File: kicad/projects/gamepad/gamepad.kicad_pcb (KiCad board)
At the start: 2 copper layers, 203.2 x 97.8 mm, 49 parts, among them J1 peripheral_addr_bus_connector, J2 peripheral_aux_connector, J3 peripheral_membank_connector, J4 Conn_01x02_Socket, J5 Conn_01x02_Socket, J6 Conn_02x05_Odd_Even, U1 74HC161, U10 74HC245, U11 74HC245, U12 74HC245, U13 74HC245, U2 74HC161, U3 74HC595, U4 74HC595, U5 74HC595, U6 74HC595, U7 74HC14, U8 74HC08, U9 74HC109

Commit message: Gamepad schematic done.
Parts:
- added C10: C, Capacitor_THT:C_Disc_D5.0mm_W2.5mm_P5.00mm, F.Cu at (116.8, 86.4)
- added C11: C, Capacitor_THT:C_Disc_D5.0mm_W2.5mm_P5.00mm, F.Cu at (129.6, 86.4)
- added C12: C, Capacitor_THT:C_Disc_D5.0mm_W2.5mm_P5.00mm, F.Cu at (182.9, 109.2)
- added C13: C, Capacitor_THT:C_Disc_D5.0mm_W2.5mm_P5.00mm, F.Cu at (215.9, 109.2)
- added C14: C, Capacitor_THT:C_Disc_D5.0mm_W2.5mm_P5.00mm, F.Cu at (147.3, 124.5)
- added J10: Pad 2 SNES, Connector_PinSocket_2.54mm:PinSocket_1x05_P2.54mm_Horizontal, F.Cu at (129.5, 61.0)
- added J11: Conn_01x03_Pin, Connector_PinHeader_2.54mm:PinHeader_1x03_P2.54mm_Horizontal, F.Cu at (52.5, 127.5)
- added J7: Pad 1 header, Connector_PinSocket_2.54mm:PinSocket_1x05_P2.54mm_Horizontal, F.Cu at (61.0, 88.9)
- added J8: Pad 1 SNES, Connector_PinSocket_2.54mm:PinSocket_1x05_P2.54mm_Horizontal, F.Cu at (81.3, 61.0)
- added J9: Pad 2 header, Connector_PinSocket_2.54mm:PinSocket_1x05_P2.54mm_Horizontal, F.Cu at (61.0, 109.2)
- added R3: 10K, Resistor_THT:R_Axial_DIN0207_L6.3mm_D2.5mm_P10.16mm_Horizontal, F.Cu at (160.0, 78.7)
- added TP1: Gamepad Latch, Connector_Pin:Pin_D1.0mm_L10.0mm, F.Cu at (-38.1, 28.5)
- added TP2: Shift out reg CLK, Connector_Pin:Pin_D1.0mm_L10.0mm, F.Cu at (-38.1, 32.5)
- added TP3: Shift Serial CLK, Connector_Pin:Pin_D1.0mm_L10.0mm, F.Cu at (-38.1, 36.6)
- added TP4: Gamepad CLK, Connector_Pin:Pin_D1.0mm_L10.0mm, F.Cu at (-38.1, 40.6)
- added TP5: Base CLK, Connector_Pin:Pin_D1.0mm_L10.0mm, F.Cu at (-34.0, 28.5)
- added TP6: ~{Base CLK}, Connector_Pin:Pin_D1.0mm_L10.0mm, F.Cu at (-34.0, 32.5)
- added TP7: RCO, Connector_Pin:Pin_D1.0mm_L10.0mm, F.Cu at (-34.0, 36.6)
- added U14: 74HC00, Package_DIP:DIP-14_W7.62mm_Socket, F.Cu at (152.4, 132.1)
- J4: value Conn_01x02_Socket -> PAD 1 ACTIVE
- J5: value Conn_01x02_Socket -> PAD 2 ACTIVE
- moved J6 21.7 mm to (81.3, 114.3), turned to 90 degrees
- moved RN2 17.8 mm to (226.1, 71.1), turned to 180 degrees
- moved U10 17.8 mm to (172.7, 86.4)
- moved RN1 15.2 mm to (190.5, 71.1), turned to 180 degrees
- moved U11 12.7 mm to (210.8, 86.4)
- moved C8 9.09 mm to (111.8, 94.0), turned to -90 degrees
- moved C7 9.09 mm to (147.3, 94.0), turned to -90 degrees
- moved C9 7.96 mm to (73.7, 94.0), turned to -90 degrees
- moved C2 7.13 mm to (111.8, 124.4)
- moved C1 5.68 mm to (73.7, 124.5)
- moved U1 5.00 mm to (78.7, 132.0)
- moved U2 5.00 mm to (116.8, 132.0)
- moved U13 2.54 mm to (221.0, 116.8)
- moved U3 2.54 mm to (193.0, 101.6)
- moved U5 2.54 mm to (193.0, 132.1)
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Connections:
- C1 pad 1: unconnected-(C1-Pad1) -> VCC
- C1 pad 2: unconnected-(C1-Pad2) -> GND
- C2 pad 1: unconnected-(C2-Pad1) -> VCC
- C2 pad 2: unconnected-(C2-Pad2) -> GND
- C3 pad 1: unconnected-(C3-Pad1) -> VCC
- C3 pad 2: unconnected-(C3-Pad2) -> GND
- C4 pad 1: unconnected-(C4-Pad1) -> VCC
- C4 pad 2: unconnected-(C4-Pad2) -> GND
- C5 pad 1: unconnected-(C5-Pad1) -> VCC
- C5 pad 2: unconnected-(C5-Pad2) -> GND
- C6 pad 1: unconnected-(C6-Pad1) -> VCC
- C6 pad 2: unconnected-(C6-Pad2) -> GND
- C7 pad 1: unconnected-(C7-Pad1) -> VCC
- C7 pad 2: unconnected-(C7-Pad2) -> GND
- C8 pad 1: unconnected-(C8-Pad1) -> VCC
- C8 pad 2: unconnected-(C8-Pad2) -> GND
- C9 pad 1: unconnected-(C9-Pad1) -> VCC
- C9 pad 2: unconnected-(C9-Pad2) -> GND
- D1 pad 1: unconnected-(D1-K-Pad1) -> Net-(D1-K)
- D1 pad 2: unconnected-(D1-A-Pad2) -> /PAD 1 LED 0
- D10 pad 1: unconnected-(D10-K-Pad1) -> Net-(D10-K)
- D10 pad 2: unconnected-(D10-A-Pad2) -> /PAD 1 LED 9
- D11 pad 1: unconnected-(D11-K-Pad1) -> Net-(D11-K)
- D11 pad 2: unconnected-(D11-A-Pad2) -> /PAD 1 LED 10
- D12 pad 1: unconnected-(D12-K-Pad1) -> Net-(D12-K)
- D12 pad 2: unconnected-(D12-A-Pad2) -> /PAD 1 LED 11
- D13 pad 1: unconnected-(D13-K-Pad1) -> /PAD 1 ADDR LED
- D13 pad 2: unconnected-(D13-A-Pad2) -> Net-(D13-A)
- D14 pad 1: unconnected-(D14-K-Pad1) -> /PAD 2 ADDR LED
- D14 pad 2: unconnected-(D14-A-Pad2) -> Net-(D14-A)
- D2 pad 1: unconnected-(D2-K-Pad1) -> Net-(D2-K)
- D2 pad 2: unconnected-(D2-A-Pad2) -> /PAD 1 LED 1
- D3 pad 1: unconnected-(D3-K-Pad1) -> Net-(D3-K)
- D3 pad 2: unconnected-(D3-A-Pad2) -> /PAD 1 LED 2
- D4 pad 1: unconnected-(D4-K-Pad1) -> Net-(D4-K)
- D4 pad 2: unconnected-(D4-A-Pad2) -> /PAD 1 LED 3
- D5 pad 1: unconnected-(D5-K-Pad1) -> Net-(D5-K)
- D5 pad 2: unconnected-(D5-A-Pad2) -> /PAD 1 LED 4
- D6 pad 1: unconnected-(D6-K-Pad1) -> Net-(D6-K)
- D6 pad 2: unconnected-(D6-A-Pad2) -> /PAD 1 LED 5
- D7 pad 1: unconnected-(D7-K-Pad1) -> Net-(D7-K)
- D7 pad 2: unconnected-(D7-A-Pad2) -> /PAD 1 LED 6
- D8 pad 1: unconnected-(D8-K-Pad1) -> Net-(D8-K)
- D8 pad 2: unconnected-(D8-A-Pad2) -> /PAD 1 LED 7
- D9 pad 1: unconnected-(D9-K-Pad1) -> Net-(D9-K)
- D9 pad 2: unconnected-(D9-A-Pad2) -> /PAD 1 LED 8
- J1 pad 17: /ADDR_BUS_00 -> unconnected-(J1-A_00-Pad17)
- J1 pad 18: /ADDR_BUS_01 -> unconnected-(J1-A_01-Pad18)
- J1 pad 19: /ADDR_BUS_02 -> unconnected-(J1-A_02-Pad19)
- J1 pad 20: /ADDR_BUS_03 -> unconnected-(J1-A_03-Pad20)
- J1 pad 21: /ADDR_BUS_04 -> unconnected-(J1-A_04-Pad21)
- J1 pad 22: /ADDR_BUS_05 -> unconnected-(J1-A_05-Pad22)
- J1 pad 23: /ADDR_BUS_06 -> unconnected-(J1-A_06-Pad23)
- J1 pad 24: /ADDR_BUS_07 -> unconnected-(J1-A_07-Pad24)
- J1 pad 25: /ADDR_BUS_08 -> unconnected-(J1-A_08-Pad25)
- J1 pad 26: /ADDR_BUS_09 -> unconnected-(J1-A_09-Pad26)
- J1 pad 27: /ADDR_BUS_10 -> unconnected-(J1-A_10-Pad27)
- J1 pad 28: /ADDR_BUS_11 -> unconnected-(J1-A_11-Pad28)
- J1 pad 29: /ADDR_BUS_12 -> unconnected-(J1-A_12-Pad29)
- J1 pad 30: /ADDR_BUS_13 -> unconnected-(J1-A_13-Pad30)
- J1 pad 31: /ADDR_BUS_14 -> unconnected-(J1-A_14-Pad31)
- J1 pad 32: /ADDR_BUS_15 -> unconnected-(J1-A_15-Pad32)
- J3 pad 1: /BANK_BUS_00 -> unconnected-(J3-B_00-Pad1)
- J3 pad 10: /BANK_BUS_09 -> unconnected-(J3-B_09-Pad10)
- J3 pad 11: /BANK_BUS_10 -> unconnected-(J3-B_10-Pad11)
- J3 pad 12: /BANK_BUS_11 -> unconnected-(J3-B_11-Pad12)
- J3 pad 13: /BANK_BUS_12 -> unconnected-(J3-B_12-Pad13)
- J3 pad 14: /BANK_BUS_13 -> unconnected-(J3-B_13-Pad14)
- J3 pad 15: /BANK_BUS_14 -> unconnected-(J3-B_14-Pad15)
- J3 pad 16: /BANK_BUS_15 -> unconnected-(J3-B_15-Pad16)
- J3 pad 2: /BANK_BUS_01 -> unconnected-(J3-B_01-Pad2)
- J3 pad 3: /BANK_BUS_02 -> unconnected-(J3-B_02-Pad3)
- J3 pad 4: /BANK_BUS_03 -> unconnected-(J3-B_03-Pad4)
- J3 pad 5: /BANK_BUS_04 -> unconnected-(J3-B_04-Pad5)
- J3 pad 6: /BANK_BUS_05 -> unconnected-(J3-B_05-Pad6)
- J3 pad 7: /BANK_BUS_06 -> unconnected-(J3-B_06-Pad7)
- J3 pad 8: /BANK_BUS_07 -> unconnected-(J3-B_07-Pad8)
- J3 pad 9: /BANK_BUS_08 -> unconnected-(J3-B_08-Pad9)
- J4 pad 1: unconnected-(J4-Pin_1-Pad1) -> /PAD 1 ACTIVE
- J4 pad 2: unconnected-(J4-Pin_2-Pad2) -> /PAD 1 ACTIVE
- J5 pad 1: unconnected-(J5-Pin_1-Pad1) -> /PAD 2 ACTIVE
- J5 pad 2: unconnected-(J5-Pin_2-Pad2) -> /PAD 2 ACTIVE
- J6 pad 1: unconnected-(J6-Pin_1-Pad1) -> /CTL_CLK
- J6 pad 10: unconnected-(J6-Pin_10-Pad10) -> /BASE CLK
- J6 pad 2: unconnected-(J6-Pin_2-Pad2) -> /BASE CLK
- J6 pad 3: unconnected-(J6-Pin_3-Pad3) -> /CLK DIV 2
- J6 pad 4: unconnected-(J6-Pin_4-Pad4) -> /BASE CLK
- J6 pad 5: unconnected-(J6-Pin_5-Pad5) -> /CLK DIV 4
- J6 pad 6: unconnected-(J6-Pin_6-Pad6) -> /BASE CLK
- J6 pad 7: unconnected-(J6-Pin_7-Pad7) -> /CLK DIV 8
- J6 pad 8: unconnected-(J6-Pin_8-Pad8) -> /BASE CLK
- J6 pad 9: unconnected-(J6-Pin_9-Pad9) -> /CLK DIV 16
- R1 pad 1: unconnected-(R1-Pad1) -> Net-(D13-A)
- R1 pad 2: unconnected-(R1-Pad2) -> VCC
- R2 pad 1: unconnected-(R2-Pad1) -> Net-(D14-A)
- R2 pad 2: unconnected-(R2-Pad2) -> VCC
- RN1 pad 1: unconnected-(RN1-common-Pad1) -> GND
- RN1 pad 2: unconnected-(RN1-R1-Pad2) -> Net-(D7-K)
- RN1 pad 3: unconnected-(RN1-R2-Pad3) -> Net-(D8-K)
- RN1 pad 4: unconnected-(RN1-R3-Pad4) -> Net-(D9-K)
- RN1 pad 5: unconnected-(RN1-R4-Pad5) -> Net-(D10-K)
- RN1 pad 6: unconnected-(RN1-R5-Pad6) -> Net-(D11-K)
- RN1 pad 7: unconnected-(RN1-R6-Pad7) -> Net-(D12-K)
- RN2 pad 1: unconnected-(RN2-common-Pad1) -> GND
- RN2 pad 2: unconnected-(RN2-R1-Pad2) -> Net-(D1-K)
- RN2 pad 3: unconnected-(RN2-R2-Pad3) -> Net-(D2-K)
- RN2 pad 4: unconnected-(RN2-R3-Pad4) -> Net-(D3-K)
- RN2 pad 5: unconnected-(RN2-R4-Pad5) -> Net-(D4-K)
- RN2 pad 6: unconnected-(RN2-R5-Pad6) -> Net-(D5-K)
- RN2 pad 7: unconnected-(RN2-R6-Pad7) -> Net-(D6-K)
- U1 pad 1: unconnected-(U1-~{MR}-Pad1) -> VCC
- U1 pad 10: unconnected-(U1-TE-Pad10) -> VCC
- U1 pad 11: unconnected-(U1-Q3-Pad11) -> /CLK DIV 16
- U1 pad 12: unconnected-(U1-Q2-Pad12) -> /CLK DIV 8
- U1 pad 13: unconnected-(U1-Q1-Pad13) -> /CLK DIV 4
- U1 pad 14: unconnected-(U1-Q0-Pad14) -> /CLK DIV 2
- U1 pad 16: unconnected-(U1-VCC-Pad16) -> VCC
- U1 pad 2: unconnected-(U1-CP-Pad2) -> /CTL_CLK
- U1 pad 7: unconnected-(U1-PE-Pad7) -> VCC
- U1 pad 8: unconnected-(U1-GND-Pad8) -> GND
- U1 pad 9: unconnected-(U1-~{SPE}-Pad9) -> VCC
- U10 pad 1: unconnected-(U10-DIR-Pad1) -> VCC
- U10 pad 10: unconnected-(U10-GND-Pad10) -> GND
- U10 pad 11: unconnected-(U10-B8-Pad11) -> /PAD 1 LED 6
- U10 pad 12: unconnected-(U10-B7-Pad12) -> /PAD 1 LED 7
- U10 pad 13: unconnected-(U10-B6-Pad13) -> /PAD 1 LED 8
- U10 pad 14: unconnected-(U10-B5-Pad14) -> /PAD 1 LED 9
- U10 pad 15: unconnected-(U10-B4-Pad15) -> /PAD 1 LED 10
- U10 pad 16: unconnected-(U10-B3-Pad16) -> /PAD 1 LED 11
- U10 pad 19: unconnected-(U10-~{OE}-Pad19) -> /~{LED ENABLE}
- U10 pad 2: unconnected-(U10-A1-Pad2) -> /PAD 1 SHIFT 15
- U10 pad 20: unconnected-(U10-VCC-Pad20) -> VCC
- U10 pad 3: unconnected-(U10-A2-Pad3) -> /PAD 1 SHIFT 14
- U10 pad 4: unconnected-(U10-A3-Pad4) -> /PAD 1 SHIFT 13
- U10 pad 5: unconnected-(U10-A3-Pad5) -> /PAD 1 SHIFT 12
- U10 pad 6: unconnected-(U10-A5-Pad6) -> /PAD 1 SHIFT 11
- U10 pad 7: unconnected-(U10-A6-Pad7) -> /PAD 1 SHIFT 10
- U10 pad 8: unconnected-(U10-A7-Pad8) -> /PAD 1 SHIFT 09
- U10 pad 9: unconnected-(U10-A8-Pad9) -> /PAD 1 SHIFT 08
- U11 pad 1: unconnected-(U11-DIR-Pad1) -> VCC
- U11 pad 10: unconnected-(U11-GND-Pad10) -> GND
- U11 pad 11: unconnected-(U11-B8-Pad11) -> /PAD 1 ADDR LED
- U11 pad 12: unconnected-(U11-B7-Pad12) -> /PAD 2 ADDR LED
- U11 pad 13: unconnected-(U11-B6-Pad13) -> /PAD 1 LED 0
- U11 pad 14: unconnected-(U11-B5-Pad14) -> /PAD 1 LED 1
- U11 pad 15: unconnected-(U11-B4-Pad15) -> /PAD 1 LED 2
- U11 pad 16: unconnected-(U11-B3-Pad16) -> /PAD 1 LED 3
- U11 pad 17: unconnected-(U11-B2-Pad17) -> /PAD 1 LED 4
- U11 pad 18: unconnected-(U11-B1-Pad18) -> /PAD 1 LED 5
- U11 pad 19: unconnected-(U11-~{OE}-Pad19) -> /~{LED ENABLE}
- U11 pad 2: unconnected-(U11-A1-Pad2) -> /PAD 1 SHIFT 07
- U11 pad 20: unconnected-(U11-VCC-Pad20) -> VCC
- U11 pad 3: unconnected-(U11-A2-Pad3) -> /PAD 1 SHIFT 06
- U11 pad 4: unconnected-(U11-A3-Pad4) -> /PAD 1 SHIFT 05
- U11 pad 5: unconnected-(U11-A3-Pad5) -> /PAD 1 SHIFT 04
- U11 pad 6: unconnected-(U11-A5-Pad6) -> /PAD 1 SHIFT 03
- U11 pad 7: unconnected-(U11-A6-Pad7) -> /PAD 1 SHIFT 02
- U11 pad 8: unconnected-(U11-A7-Pad8) -> /PAD 1 SHIFT 01
- U11 pad 9: unconnected-(U11-A8-Pad9) -> /PAD 1 SHIFT 00
- U12 pad 1: unconnected-(U12-DIR-Pad1) -> GND
- U12 pad 10: unconnected-(U12-GND-Pad10) -> GND
- U12 pad 11: unconnected-(U12-B8-Pad11) -> /PAD 1 SHIFT 08
- U12 pad 12: unconnected-(U12-B7-Pad12) -> /PAD 1 SHIFT 09
- U12 pad 13: unconnected-(U12-B6-Pad13) -> /PAD 1 SHIFT 10
- U12 pad 14: unconnected-(U12-B5-Pad14) -> /PAD 1 SHIFT 11
- U12 pad 15: unconnected-(U12-B4-Pad15) -> /PAD 1 SHIFT 12
- U12 pad 16: unconnected-(U12-B3-Pad16) -> /PAD 1 SHIFT 13
- U12 pad 17: unconnected-(U12-B2-Pad17) -> /PAD 1 SHIFT 14
- U12 pad 18: unconnected-(U12-B1-Pad18) -> /PAD 1 SHIFT 15
- U12 pad 19: unconnected-(U12-~{OE}-Pad19) -> /PAD 1 ~{OE}
- U12 pad 2: unconnected-(U12-A1-Pad2) -> /DATA_BUS_15
- U12 pad 20: unconnected-(U12-VCC-Pad20) -> VCC
- U12 pad 3: unconnected-(U12-A2-Pad3) -> /DATA_BUS_14
- U12 pad 4: unconnected-(U12-A3-Pad4) -> /DATA_BUS_13
- U12 pad 5: unconnected-(U12-A3-Pad5) -> /DATA_BUS_12
- U12 pad 6: unconnected-(U12-A5-Pad6) -> /DATA_BUS_11
- U12 pad 7: unconnected-(U12-A6-Pad7) -> /DATA_BUS_10
- U12 pad 8: unconnected-(U12-A7-Pad8) -> /DATA_BUS_09
- U12 pad 9: unconnected-(U12-A8-Pad9) -> /DATA_BUS_08
- U13 pad 1: unconnected-(U13-DIR-Pad1) -> GND
- U13 pad 10: unconnected-(U13-GND-Pad10) -> GND
- U13 pad 11: unconnected-(U13-B8-Pad11) -> /PAD 1 SHIFT 00
- U13 pad 12: unconnected-(U13-B7-Pad12) -> /PAD 1 SHIFT 01
- U13 pad 13: unconnected-(U13-B6-Pad13) -> /PAD 1 SHIFT 02
- U13 pad 14: unconnected-(U13-B5-Pad14) -> /PAD 1 SHIFT 03
- U13 pad 15: unconnected-(U13-B4-Pad15) -> /PAD 1 SHIFT 04
- U13 pad 16: unconnected-(U13-B3-Pad16) -> /PAD 1 SHIFT 05
- U13 pad 17: unconnected-(U13-B2-Pad17) -> /PAD 1 SHIFT 06
- U13 pad 18: unconnected-(U13-B1-Pad18) -> /PAD 1 SHIFT 07
- U13 pad 19: unconnected-(U13-~{OE}-Pad19) -> /PAD 1 ~{OE}
- U13 pad 2: unconnected-(U13-A1-Pad2) -> /DATA_BUS_07
- U13 pad 20: unconnected-(U13-VCC-Pad20) -> VCC
- U13 pad 3: unconnected-(U13-A2-Pad3) -> /DATA_BUS_06
- U13 pad 4: unconnected-(U13-A3-Pad4) -> /DATA_BUS_05
- U13 pad 5: unconnected-(U13-A3-Pad5) -> /DATA_BUS_04
- U13 pad 6: unconnected-(U13-A5-Pad6) -> /DATA_BUS_03
- U13 pad 7: unconnected-(U13-A6-Pad7) -> /DATA_BUS_02
- U13 pad 8: unconnected-(U13-A7-Pad8) -> /DATA_BUS_01
- U13 pad 9: unconnected-(U13-A8-Pad9) -> /DATA_BUS_00
- U2 pad 1: unconnected-(U2-~{MR}-Pad1) -> VCC
- U2 pad 10: unconnected-(U2-TE-Pad10) -> VCC
- U2 pad 15: unconnected-(U2-TC-Pad15) -> Net-(U2-TC)
- U2 pad 16: unconnected-(U2-VCC-Pad16) -> VCC
- U2 pad 2: unconnected-(U2-CP-Pad2) -> /SHIFT SERIAL CLK
- U2 pad 3: unconnected-(U2-P0-Pad3) -> GND
- U2 pad 4: unconnected-(U2-P1-Pad4) -> GND
- U2 pad 5: unconnected-(U2-P2-Pad5) -> GND
- U2 pad 6: unconnected-(U2-P3-Pad6) -> GND
- U2 pad 7: unconnected-(U2-PE-Pad7) -> VCC
- U2 pad 8: unconnected-(U2-GND-Pad8) -> GND
- U2 pad 9: unconnected-(U2-~{SPE}-Pad9) -> VCC
- U3 pad 1: unconnected-(U3-QB-Pad1) -> /PAD 1 SHIFT 14
- U3 pad 10: unconnected-(U3-~{SRCLR}-Pad10) -> VCC
- U3 pad 11: unconnected-(U3-SRCLK-Pad11) -> /SHIFT SERIAL CLK
- U3 pad 12: unconnected-(U3-RCLK-Pad12) -> /SHIFT OUT REG CLK
- U3 pad 13: unconnected-(U3-~{OE}-Pad13) -> GND
- U3 pad 14: unconnected-(U3-SER-Pad14) -> Net-(U3-SER)
- U3 pad 15: unconnected-(U3-QA-Pad15) -> /PAD 1 SHIFT 15
- U3 pad 16: unconnected-(U3-VCC-Pad16) -> VCC
- U3 pad 2: unconnected-(U3-QC-Pad2) -> /PAD 1 SHIFT 13
- U3 pad 3: unconnected-(U3-QD-Pad3) -> /PAD 1 SHIFT 12
- U3 pad 4: unconnected-(U3-QE-Pad4) -> /PAD 1 SHIFT 11
- U3 pad 5: unconnected-(U3-QF-Pad5) -> /PAD 1 SHIFT 10
- U3 pad 6: unconnected-(U3-QG-Pad6) -> /PAD 1 SHIFT 09
- U3 pad 7: unconnected-(U3-QH-Pad7) -> /PAD 1 SHIFT 08
- U3 pad 8: unconnected-(U3-GND-Pad8) -> GND
- U3 pad 9: unconnected-(U3-QH'-Pad9) -> Net-(U3-QH')
- U4 pad 1: unconnected-(U4-QB-Pad1) -> /PAD 1 SHIFT 06
- U4 pad 10: unconnected-(U4-~{SRCLR}-Pad10) -> VCC
- U4 pad 11: unconnected-(U4-SRCLK-Pad11) -> /SHIFT SERIAL CLK
- U4 pad 12: unconnected-(U4-RCLK-Pad12) -> /SHIFT OUT REG CLK
- U4 pad 13: unconnected-(U4-~{OE}-Pad13) -> GND
- U4 pad 14: unconnected-(U4-SER-Pad14) -> Net-(U3-QH')
- U4 pad 15: unconnected-(U4-QA-Pad15) -> /PAD 1 SHIFT 07
- U4 pad 16: unconnected-(U4-VCC-Pad16) -> VCC
- U4 pad 2: unconnected-(U4-QC-Pad2) -> /PAD 1 SHIFT 05
- U4 pad 3: unconnected-(U4-QD-Pad3) -> /PAD 1 SHIFT 04
- U4 pad 4: unconnected-(U4-QE-Pad4) -> /PAD 1 SHIFT 03
- U4 pad 5: unconnected-(U4-QF-Pad5) -> /PAD 1 SHIFT 02
- U4 pad 6: unconnected-(U4-QG-Pad6) -> /PAD 1 SHIFT 01
- U4 pad 7: unconnected-(U4-QH-Pad7) -> /PAD 1 SHIFT 00
- U4 pad 8: unconnected-(U4-GND-Pad8) -> GND
- U5 pad 1: unconnected-(U5-QB-Pad1) -> /DATA_BUS_14
- U5 pad 10: unconnected-(U5-~{SRCLR}-Pad10) -> VCC
- U5 pad 11: unconnected-(U5-SRCLK-Pad11) -> /SHIFT SERIAL CLK
- U5 pad 12: unconnected-(U5-RCLK-Pad12) -> /SHIFT OUT REG CLK
- U5 pad 13: unconnected-(U5-~{OE}-Pad13) -> /PAD 2 ~{OE}
- U5 pad 14: unconnected-(U5-SER-Pad14) -> Net-(U5-SER)
- U5 pad 15: unconnected-(U5-QA-Pad15) -> /DATA_BUS_15
- U5 pad 16: unconnected-(U5-VCC-Pad16) -> VCC
- U5 pad 2: unconnected-(U5-QC-Pad2) -> /DATA_BUS_13
- U5 pad 3: unconnected-(U5-QD-Pad3) -> /DATA_BUS_12
- U5 pad 4: unconnected-(U5-QE-Pad4) -> /DATA_BUS_11
- U5 pad 5: unconnected-(U5-QF-Pad5) -> /DATA_BUS_10
- U5 pad 6: unconnected-(U5-QG-Pad6) -> /DATA_BUS_09
- U5 pad 7: unconnected-(U5-QH-Pad7) -> /DATA_BUS_08
- U5 pad 8: unconnected-(U5-GND-Pad8) -> GND
- U5 pad 9: unconnected-(U5-QH'-Pad9) -> Net-(U5-QH')
- U6 pad 1: unconnected-(U6-QB-Pad1) -> /DATA_BUS_06
- U6 pad 10: unconnected-(U6-~{SRCLR}-Pad10) -> VCC
- U6 pad 11: unconnected-(U6-SRCLK-Pad11) -> /SHIFT SERIAL CLK
- U6 pad 12: unconnected-(U6-RCLK-Pad12) -> /SHIFT OUT REG CLK
- U6 pad 13: unconnected-(U6-~{OE}-Pad13) -> /PAD 2 ~{OE}
- U6 pad 14: unconnected-(U6-SER-Pad14) -> Net-(U5-QH')
- U6 pad 15: unconnected-(U6-QA-Pad15) -> /DATA_BUS_07
- U6 pad 16: unconnected-(U6-VCC-Pad16) -> VCC
- U6 pad 2: unconnected-(U6-QC-Pad2) -> /DATA_BUS_05
- U6 pad 3: unconnected-(U6-QD-Pad3) -> /DATA_BUS_04
- U6 pad 4: unconnected-(U6-QE-Pad4) -> /DATA_BUS_03
- U6 pad 5: unconnected-(U6-QF-Pad5) -> /DATA_BUS_02
- U6 pad 6: unconnected-(U6-QG-Pad6) -> /DATA_BUS_01
- U6 pad 7: unconnected-(U6-QH-Pad7) -> /DATA_BUS_00
- U6 pad 8: unconnected-(U6-GND-Pad8) -> GND
- U7 pad 1: unconnected-(U7-Pad1) -> /BASE CLK
- U7 pad 11: unconnected-(U7-Pad11) -> GND
- U7 pad 13: unconnected-(U7-Pad13) -> GND
- U7 pad 14: unconnected-(U7G-VCC-Pad14) -> VCC
- U7 pad 2: unconnected-(U7-Pad2) -> /~{BASE CLK}
- U7 pad 3: unconnected-(U7-Pad3) -> /PAD 1 DATA
- U7 pad 4: unconnected-(U7-Pad4) -> Net-(U3-SER)
- U7 pad 5: unconnected-(U7-Pad5) -> /PAD 2 DATA
- U7 pad 6: unconnected-(U7-Pad6) -> Net-(U5-SER)
- U7 pad 7: unconnected-(U7G-GND-Pad7) -> GND
- U7 pad 9: unconnected-(U7-Pad9) -> GND
- U8 pad 1: unconnected-(U8-Pad1) -> Net-(U2-TC)
- U8 pad 10: unconnected-(U8-Pad10) -> Net-(U8-Pad10)
- U8 pad 12: unconnected-(U8-Pad12) -> GND
- U8 pad 13: unconnected-(U8-Pad13) -> GND
- U8 pad 14: unconnected-(U8E-VCC-Pad14) -> VCC
- U8 pad 2: unconnected-(U8-Pad2) -> /GAMEPAD CLK
- U8 pad 3: unconnected-(U8-Pad3) -> Net-(U8-Pad10)
- U8 pad 4: unconnected-(U8-Pad4) -> /~{BASE CLK}
- U8 pad 5: unconnected-(U8-Pad5) -> Net-(U8-Pad10)
- U8 pad 6: unconnected-(U8-Pad6) -> /GAMEPAD LATCH
- U8 pad 7: unconnected-(U8E-GND-Pad7) -> GND
- U8 pad 8: unconnected-(U8-Pad8) -> /SHIFT OUT REG CLK
- U8 pad 9: unconnected-(U8-Pad9) -> /BASE CLK
- U9 pad 1: unconnected-(U9A-~{CLR}-Pad1) -> VCC
- U9 pad 11: unconnected-(U9B-~{PRE}-Pad11) -> VCC
- U9 pad 12: unconnected-(U9B-C-Pad12) -> GND
- U9 pad 13: unconnected-(U9B-~{K}-Pad13) -> GND
- U9 pad 14: unconnected-(U9B-J-Pad14) -> GND
- U9 pad 15: unconnected-(U9B-~{CLR}-Pad15) -> VCC
- U9 pad 16: unconnected-(U9C-VCC-Pad16) -> VCC
- U9 pad 2: unconnected-(U9A-J-Pad2) -> VCC
- U9 pad 3: unconnected-(U9A-~{K}-Pad3) -> GND
- U9 pad 4: unconnected-(U9A-C-Pad4) -> /BASE CLK
- U9 pad 5: unconnected-(U9A-~{PRE}-Pad5) -> VCC
- U9 pad 6: unconnected-(U9A-Q-Pad6) -> /SHIFT SERIAL CLK
- U9 pad 7: unconnected-(U9A-~{Q}-Pad7) -> /GAMEPAD CLK
- U9 pad 8: unconnected-(U9C-GND-Pad8) -> GND

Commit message: Start routing gamepad PCB.
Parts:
- added R4: 10K, Resistor_THT:R_Axial_DIN0207_L6.3mm_D2.5mm_P10.16mm_Horizontal, F.Cu at (106.7, 111.8)
- added TP8: Raw Gamepad Latch, Connector_Pin:Pin_D1.0mm_L10.0mm, F.Cu at (108.5, 76.7)
- added TP9: Raw Shift out reg CLK, Connector_Pin:Pin_D1.0mm_L10.0mm, F.Cu at (113.0, 81.5)
- U8: value 74HC08 -> 74HC00
- U9: value 74HC109 -> 74HC161
- moved TP4 150.3 mm to (106.7, 81.0), turned to 90 degrees
- moved TP3 147.6 mm to (102.6, 81.0), turned to 90 degrees
- moved TP2 145.0 mm to (98.6, 81.0), turned to 90 degrees
- moved TP1 142.7 mm to (94.5, 81.0), turned to 90 degrees
- moved TP7 142.5 mm to (102.6, 77.0), turned to 90 degrees
- moved TP6 139.9 mm to (98.6, 77.0), turned to 90 degrees
- moved TP5 137.4 mm to (94.5, 77.0), turned to 90 degrees
- moved U8 46.8 mm to (152.4, 132.1)
- moved C10 38.2 mm to (154.9, 88.9), turned to 90 degrees
- moved U14 35.6 mm to (116.8, 132.1)
- moved C11 30.5 mm to (160.0, 88.9), turned to 90 degrees
- moved U2 30.4 mm to (116.8, 101.6)
- moved R3 30.0 mm to (140.0, 56.4), turned to 0 degrees
- moved J11 13.1 mm to (63.5, 134.6), turned to 180 degrees
- moved C2 0.08 mm to (111.8, 124.5)
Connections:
- C10 pad 1: /GAMEPAD LATCH -> Net-(C10-Pad1)
- C11 pad 1: /SHIFT OUT REG CLK -> Net-(C11-Pad1)
- U14 pad 1: /PAD 2 ACTIVE -> Net-(U14-Pad1)
- U14 pad 10: GND -> Net-(U14-Pad10)
- U14 pad 11: unconnected-(U14-Pad11) -> Net-(C11-Pad1)
- U14 pad 12: GND -> /BASE CLK
- U14 pad 13: GND -> Net-(U14-Pad10)
- U14 pad 2: /RFM -> Net-(U14-Pad1)
- U14 pad 3: /PAD 2 ~{OE} -> Net-(U14-Pad10)
- U14 pad 4: /RFM -> Net-(U2-TC)
- U14 pad 5: /PAD 1 ACTIVE -> /GAMEPAD CLK
- U14 pad 6: /PAD 1 ~{OE} -> Net-(U14-Pad1)
- U14 pad 8: unconnected-(U14-Pad8) -> Net-(C10-Pad1)
- U14 pad 9: GND -> /~{BASE CLK}
- U7 pad 10: unconnected-(U7-Pad10) -> /SHIFT OUT REG CLK
- U7 pad 11: GND -> Net-(C11-Pad1)
- U7 pad 12: unconnected-(U7-Pad12) -> /GAMEPAD LATCH
- U7 pad 13: GND -> Net-(C10-Pad1)
- U7 pad 8: unconnected-(U7-Pad8) -> /GAMEPAD CLK
- U7 pad 9: GND -> /SHIFT SERIAL CLK
- U8 pad 1: Net-(U2-TC) -> /PAD 2 ACTIVE
- U8 pad 10: Net-(U8-Pad10) -> GND
- U8 pad 2: /GAMEPAD CLK -> /RFM
- U8 pad 3: Net-(U8-Pad10) -> /PAD 2 ~{OE}
- U8 pad 4: /~{BASE CLK} -> /RFM
- U8 pad 5: Net-(U8-Pad10) -> /PAD 1 ACTIVE
- U8 pad 6: /GAMEPAD LATCH -> /PAD 1 ~{OE}
- U8 pad 8: /SHIFT OUT REG CLK -> unconnected-(U8-Pad8)
- U8 pad 9: /BASE CLK -> GND
- U9 pad 10: unconnected-(U9B-Q-Pad10) -> VCC
- U9 pad 11: VCC -> unconnected-(U9-Q3-Pad11)
- U9 pad 12: GND -> unconnected-(U9-Q2-Pad12)
- U9 pad 13: GND -> unconnected-(U9-Q1-Pad13)
- U9 pad 14: GND -> /SHIFT SERIAL CLK
- U9 pad 15: VCC -> unconnected-(U9-TC-Pad15)
- U9 pad 2: VCC -> /BASE CLK
- U9 pad 4: /BASE CLK -> GND
- U9 pad 5: VCC -> GND
- U9 pad 6: /SHIFT SERIAL CLK -> GND
- U9 pad 7: /GAMEPAD CLK -> VCC
- U9 pad 9: unconnected-(U9B-~{Q}-Pad9) -> VCC
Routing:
- net VCC: track 0.00 -> 553.3 mm, vias 0 -> 16
- net /SHIFT SERIAL CLK: track 0.00 -> 224.6 mm, vias 0 -> 10
- net /PAD 1 ACTIVE: track 0.00 -> 166.5 mm, vias 0 -> 4
- net /PAD 2 ACTIVE: track 0.00 -> 144.1 mm, vias 0 -> 4
- net /BASE CLK: track 0.00 -> 107.6 mm, vias 0 -> 4
- net /RFM: track 0.00 -> 104.7 mm, vias 0 -> 4
- net /GAMEPAD CLK: track 0.00 -> 99.9 mm, vias 0 -> 2
- net /SHIFT OUT REG CLK: track 0.00 -> 82.9 mm, vias 0 -> 5
- net Net-(C11-Pad1): track 0.00 -> 61.2 mm, vias 0 -> 3
- net Net-(U3-SER): track 0.00 -> 51.1 mm, vias 0 -> 4
- net Net-(C10-Pad1): track 0.00 -> 49.6 mm, vias 0 -> 3
- net /PAD 2 ~{OE}: track 0.00 -> 49.0 mm, vias 0 -> 3
- net /PAD 1 SHIFT 07: track 0.00 -> 46.9 mm, vias 0 -> 3
- net /~{BASE CLK}: track 0.00 -> 46.5 mm, vias 0 -> 3
- net Net-(U2-TC): track 0.00 -> 45.9 mm, vias 0 -> 3
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
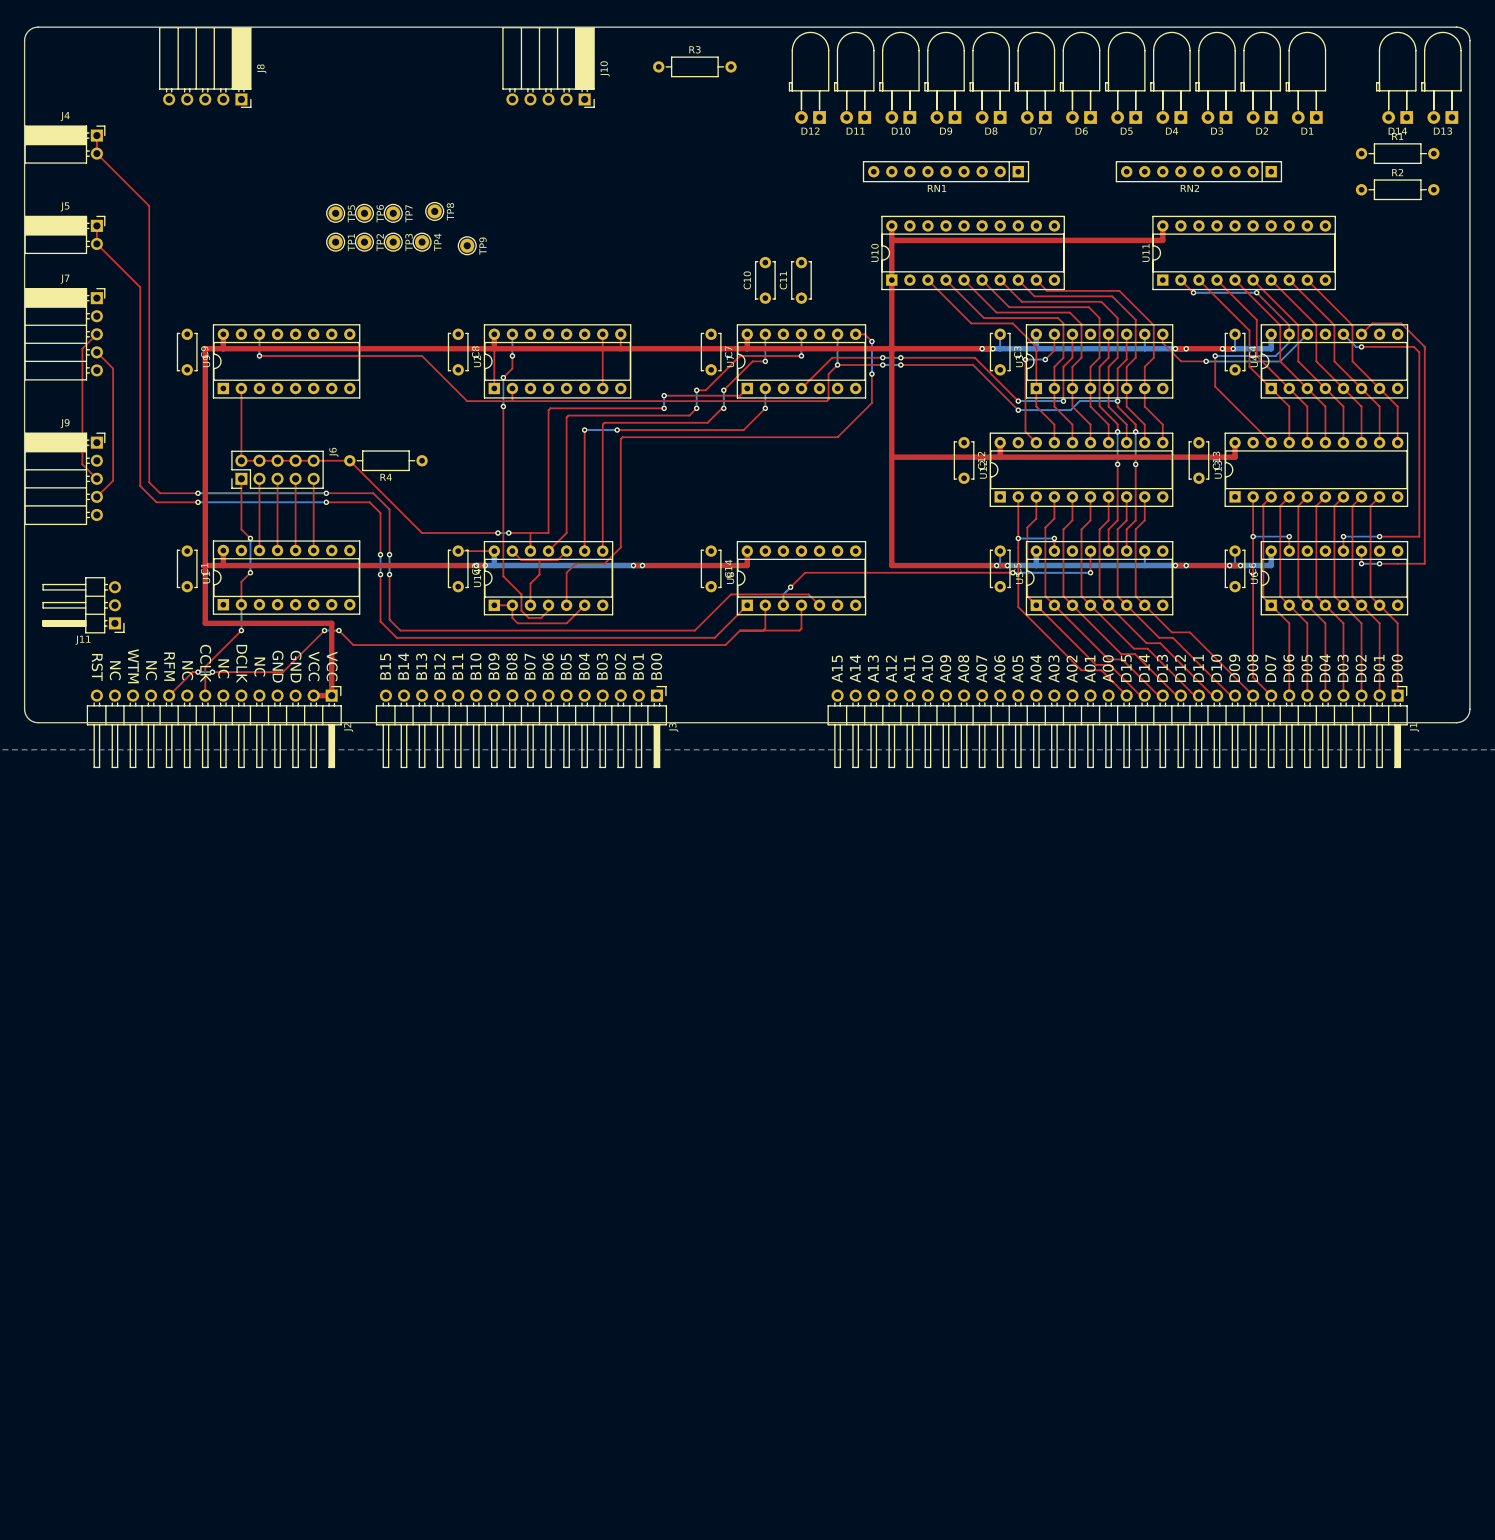
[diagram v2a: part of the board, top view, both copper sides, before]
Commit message: More PCB work on gamepad.
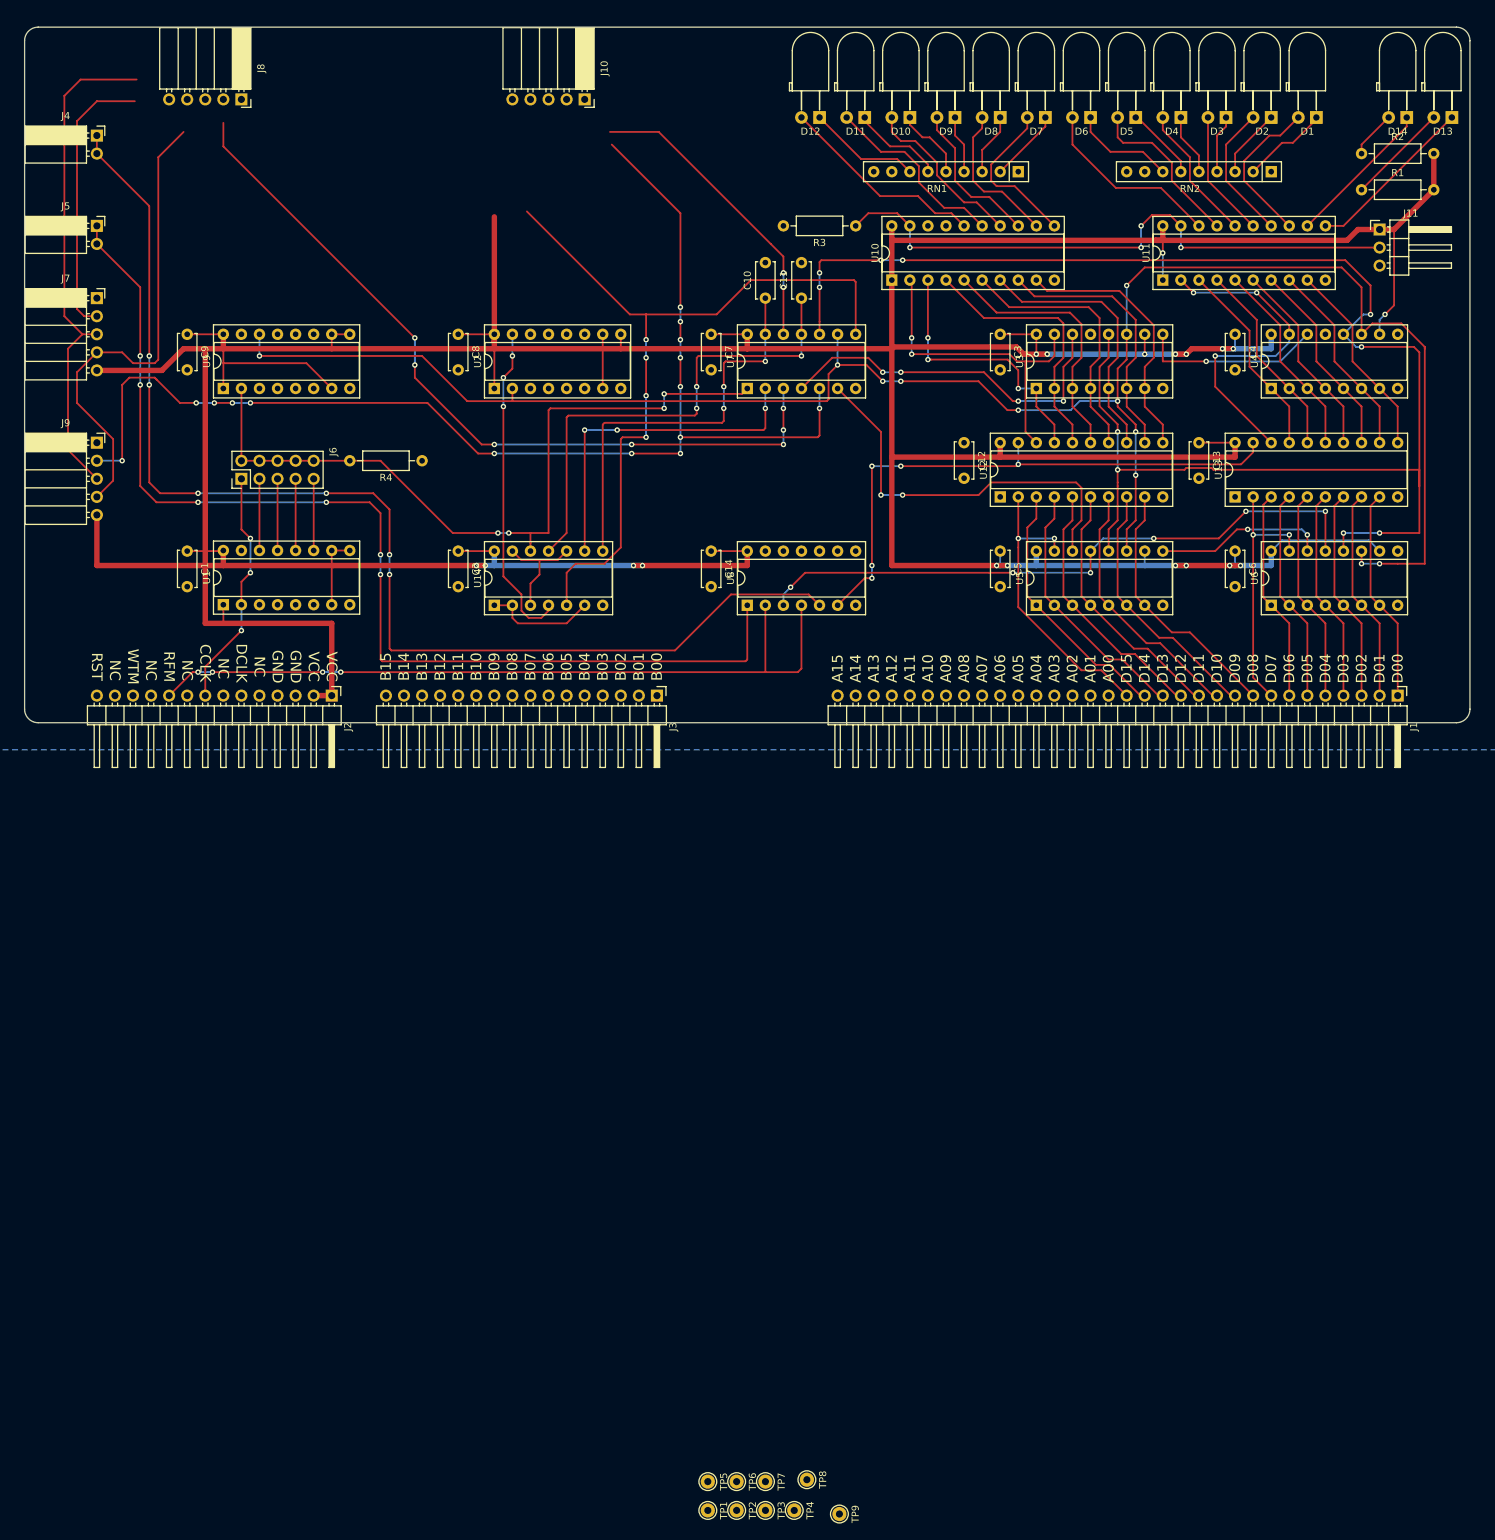
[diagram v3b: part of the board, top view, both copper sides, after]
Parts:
- moved J11 186.2 mm to (241.3, 79.2), turned to 0 degrees
- moved TP1 185.8 mm to (146.9, 259.3)
- moved TP2 185.8 mm to (150.9, 259.3)
- moved TP3 185.8 mm to (155.0, 259.3)
- moved TP4 185.8 mm to (159.0, 259.3)
- moved TP5 185.8 mm to (146.9, 255.3)
- moved TP6 185.8 mm to (150.9, 255.3)
- moved TP7 185.8 mm to (155.0, 255.3)
- moved TP8 185.8 mm to (160.8, 255.0)
- moved TP9 185.8 mm to (165.4, 259.8)
- moved R3 35.6 mm to (167.6, 78.7), turned to 180 degrees
- moved R1 5.08 mm to (238.8, 73.7)
- moved R2 5.08 mm to (238.8, 68.6)
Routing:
- net VCC: track 553.3 -> 769.8 mm, vias 16 -> 19
- net /PAD 2 DATA: track 0.00 -> 171.2 mm, vias 0 -> 15
- net /PAD 1 DATA: track 0.00 -> 149.5 mm, vias 0 -> 7
- net /SHIFT OUT REG CLK: track 82.9 -> 226.1 mm, vias 5 -> 10
- net /GAMEPAD LATCH: track 22.0 -> 113.1 mm, vias 0 -> 2
- net /~{LED ENABLE}: track 0.00 -> 85.5 mm, vias 0 -> 4
- net /PAD 1 ~{OE}: track 0.00 -> 81.0 mm, vias 0 -> 5
- net /GAMEPAD CLK: track 99.9 -> 179.0 mm, vias 2 -> 4
- net Net-(U5-SER): track 0.00 -> 56.2 mm, vias 0 -> 2
- net /SHIFT SERIAL CLK: track 224.6 -> 273.3 mm, vias 10 -> 11
- net /PAD 2 ~{OE}: track 49.0 -> 89.9 mm, vias 3 -> 6
- net /PAD 1 LED 11: track 0.00 -> 29.2 mm
- net /PAD 1 SHIFT 15: track 19.2 -> 46.4 mm
- net /PAD 1 LED 10: track 0.00 -> 26.7 mm
- net /PAD 1 LED 5: track 0.00 -> 26.3 mm
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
